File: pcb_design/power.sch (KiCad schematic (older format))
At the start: 0 parts

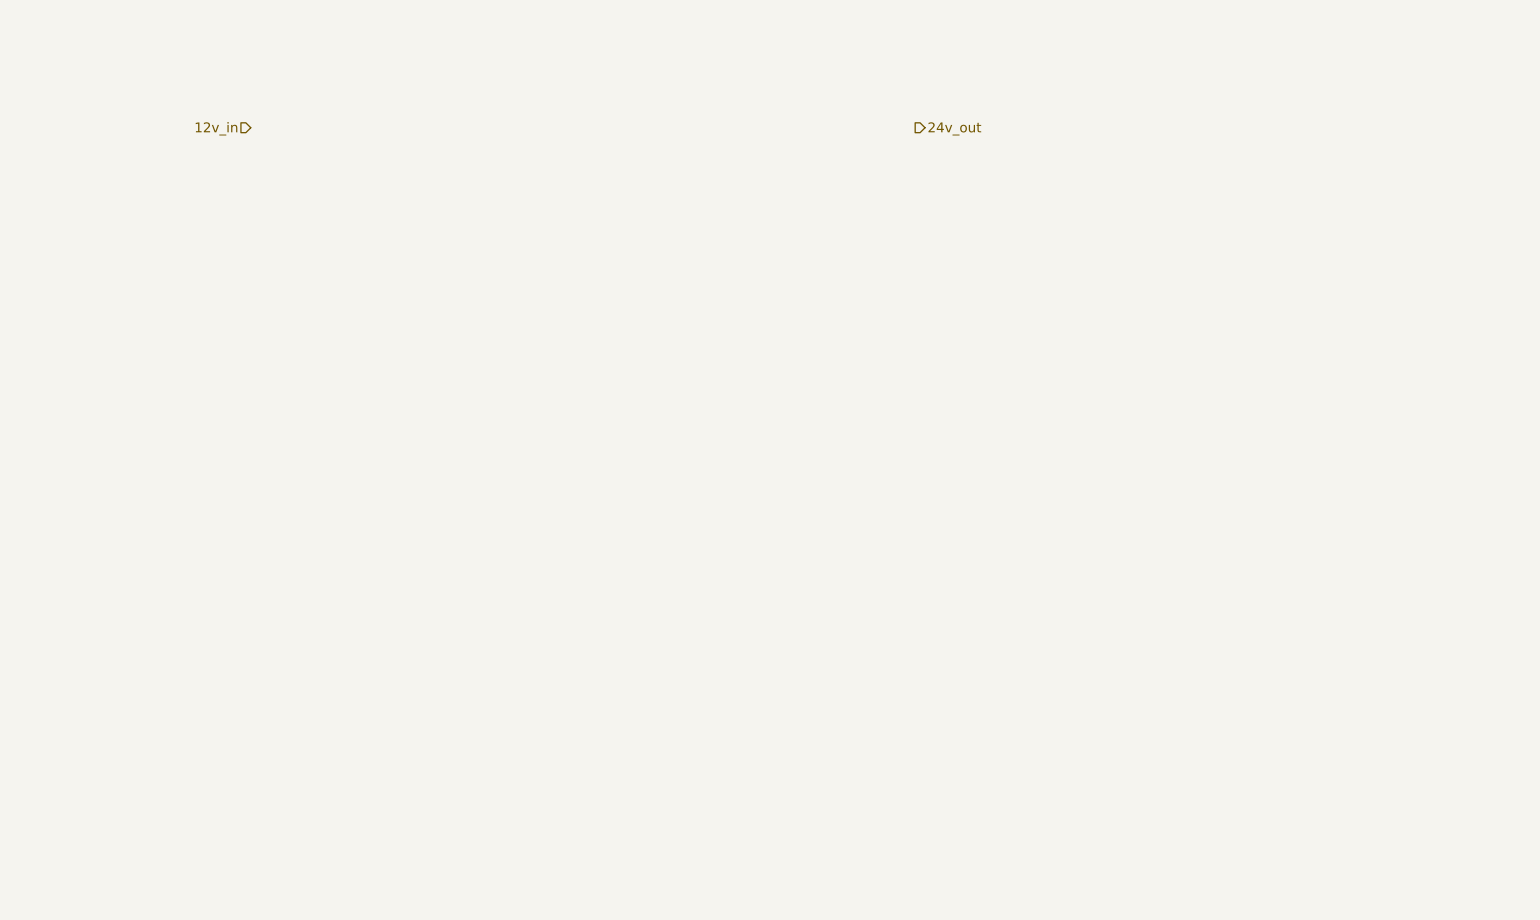
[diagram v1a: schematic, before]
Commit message: Added terminal blocks and power supplies
Signed-off-by: Marcos Chaparro <mchaparro@paltatech.com>
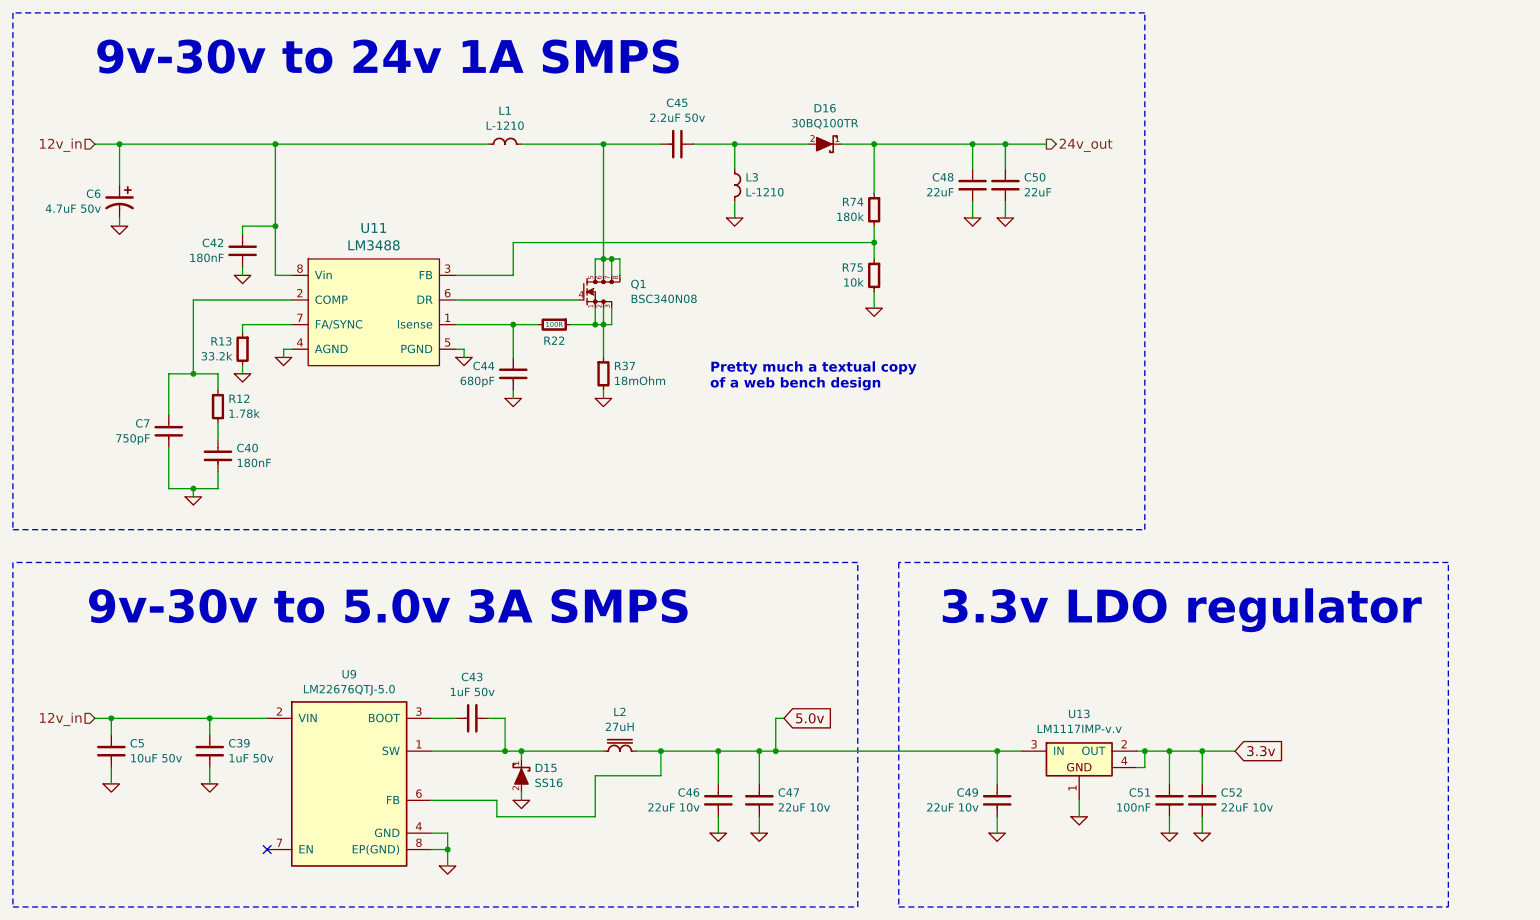
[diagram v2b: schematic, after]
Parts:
- added C39, C43: 1uF 50v, IPC7351-Nominal:CAPC2012X70, symbol C-0805
- added C40, C42: 180nF, IPC7351-Nominal:CAPC1608X55, symbol C-0603
- added C44: 680pF, IPC7351-Nominal:CAPC2012X70, symbol C-0805
- added C45: 2.2uF 50v, IPC7351-Nominal:CAPC3216X70, symbol C-1206
- added C46, C47, C49, C52: 22uF 10v, IPC7351-Nominal:CAPC3216X70, symbol C-1206
- added C48, C50: 22uF, IPC7351-Nominal:CAPC2012X70, symbol C-0805
- added C5: 10uF 50v, IPC7351-Nominal:CAPC3216X70, symbol C-1206
- added C51: 100nF, IPC7351-Nominal:CAPC1608X55, symbol C-0603
- added C6: 4.7uF 50v, IPC7351-Nominal:CAPMP7343X310, symbol C-TANT-7343-31
- added C7: 750pF, IPC7351-Nominal:CAPC2012X70, symbol C-0805
- added D15: SS16, IPC7351-Nominal:DIOM5326X292, symbol SS16
- added D16: 30BQ100TR, IPC7351-Nominal:DIOM7959X265, symbol MBRS360
- added L1, L3: L-1210, IPC7351-Nominal:INDC3225X135, symbol L-1210
- added L2: 27uH, manuf:BOURNS-SRP1238A, symbol L-BOURNS-SRN1060
- added Q1: BSC340N08, manuf:TEXAS-Q5A, symbol CSD18503Q5A
- added R12: 1.78k, IPC7351-Nominal:RESC1608X50, symbol R-0603
- added R13: 33.2k, IPC7351-Nominal:RESC1608X50, symbol R-0603
- added R22: 100R, IPC7351-Nominal:RESC1608X50, symbol R-0603
- added R37: 18mOhm, IPC7351-Nominal:CAPC1632X76, symbol R-0612
- added R74: 180k, IPC7351-Nominal:RESC1608X50, symbol R-0603
- added R75: 10k, IPC7351-Nominal:RESC1608X50, symbol R-0603
- added U11: LM3488, IPC7351-Nominal:SOP65P490X109-8, symbol LM3488
- added U13: LM1117IMP-v.v, smd-semi:SOT-223, symbol LM1117IMP-v.v
- added U9: LM22676QTJ-5.0, manuf:TO-263-7-TEXAS, symbol LM22676QTJ-5.0
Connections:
- net 12v_in: now also C39.1, C42.1, C5.1, C6.1, L1.2, U11.8 (Vin), U9.2 (VIN)
- net 24v_out: now also C48.1, C50.1, D16.1 (K), R74.1
- new net: C44.1, R22.2, U11.1 (Isense)
- new net: C7.1, R12.1, U11.2 (COMP)
- new net: R74.2, R75.1, U11.3 (FB)
- new net: Q1.4 (G), U11.6 (DR)
- new net: R13.1, U11.7 (FA/SYNC)
- new net: C40.1, R12.2
- new net: Q1.1 (S), Q1.2 (S), Q1.3 (S), R22.1, R37.1
- new net: C45.2, L1.1, Q1.5 (D), Q1.6 (D), Q1.7 (D), Q1.8 (D)
- new net: C45.1, D16.2 (A), L3.2
- new net: C43.1, D15.1 (K), L2.2, U9.1 (SW)
- new net: C43.2, U9.3 (BOOT)
- new net 3.3v: C51.1, C52.2, U13.2 (OUT), U13.4
- new net 5.0v: C46.1, C47.1, C49.1, L2.1, U13.3 (IN), U9.6 (FB)
- new net GND: C39.2, C40.2, C42.2, C44.2, C46.2, C47.2, C48.2, C49.2, C5.2, C50.2, C51.2, C52.1, C6.2, C7.2, D15.2 (A), L3.1, R13.2, R37.2, R75.2, U11.4 (AGND), U11.5 (PGND), U13.1, U9.4 (GND), U9.8 (EP(GND))
- no-connect marks 0 -> 1
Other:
- note added: "3.3v LDO regulator"
- note added: "9v-30v to 24v 1A SMPS"
- note added: "9v-30v to 5.0v 3A SMPS"
- note added: "Pretty much a textual copy\nof a web bench design"

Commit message: Added lp filters, fuses, tvs and power symbols
Signed-off-by: Marcos Chaparro <mchaparro@paltatech.com>
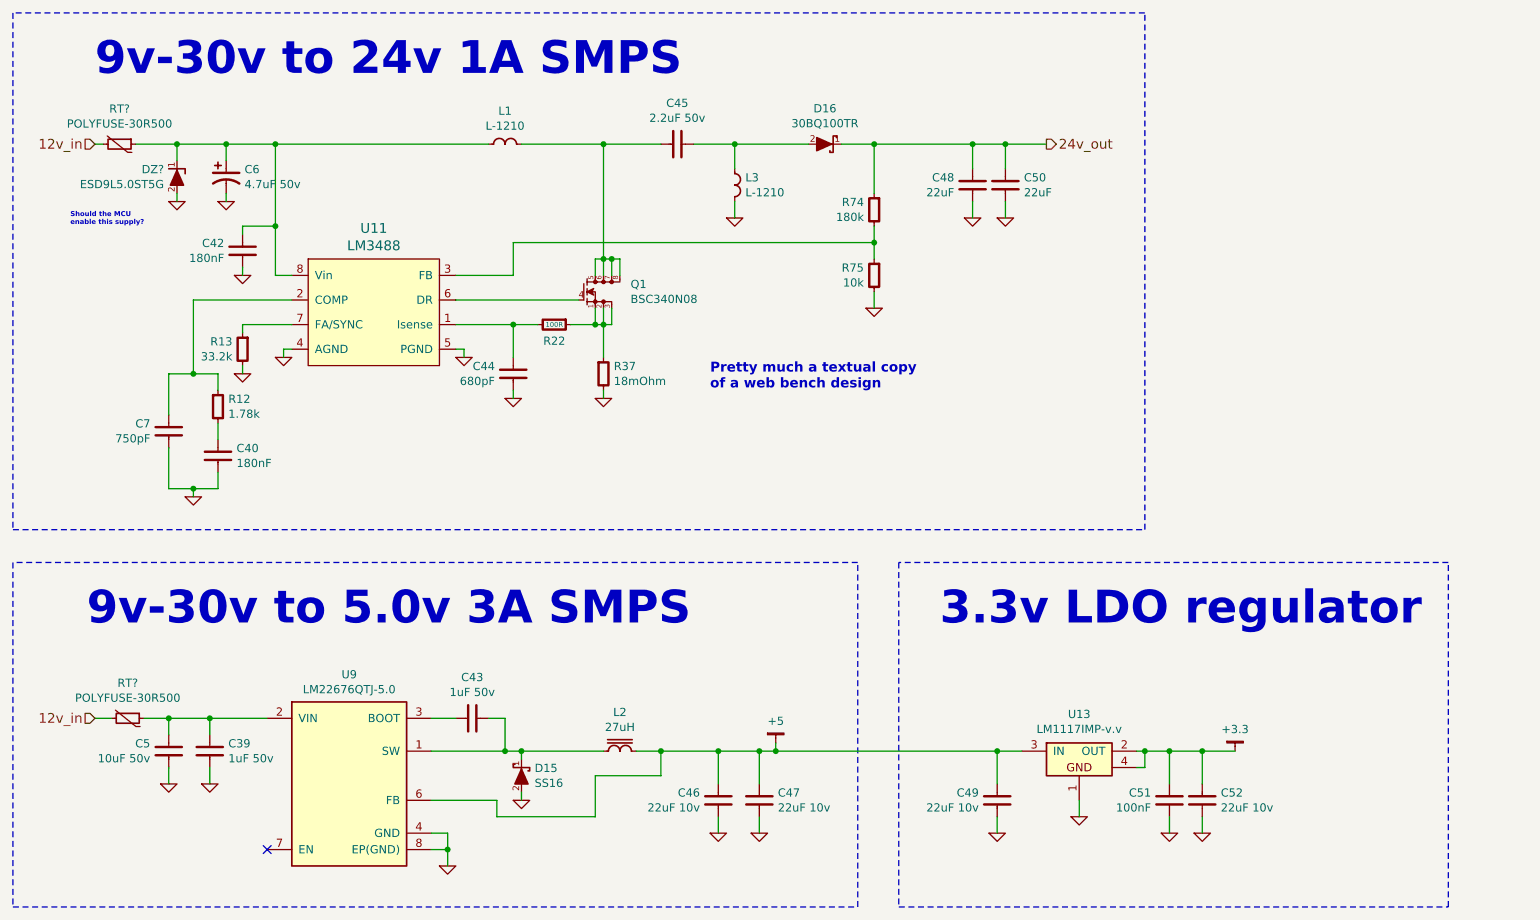
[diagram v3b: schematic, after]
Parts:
- added DZ?: ESD9L5.0ST5G, smd-semi:SOD-THAT, symbol ESD9L5.0ST5G
- added RT? (x2): POLYFUSE-30R500, manuf:LITTELFUSE-30R500, symbol POLYFUSE-30R500
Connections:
- net 12v_in: now also RT?.2, RT?.2; no longer C39.1, C42.1, C5.1, C6.1, L1.2, U11.8 (Vin), U9.2 (VIN)
- net GND: now also DZ?.2 (A)
- net 3.3v renamed +3.3
- net 5.0v renamed +5
- new net: C42.1, C6.1, DZ?.1 (K), L1.2, RT?.1, U11.8 (Vin)
- new net: C39.1, C5.1, RT?.1, U9.2 (VIN)
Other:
- note added: "Should the MCU\nenable this supply?"
- moved on the sheet: C5, C6

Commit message: Added bus voltage conditioning, %v to accel and regen inputs, regulator diode, annotated schematic
Signed-off-by: Marcos Chaparro <mchaparro@paltatech.com>
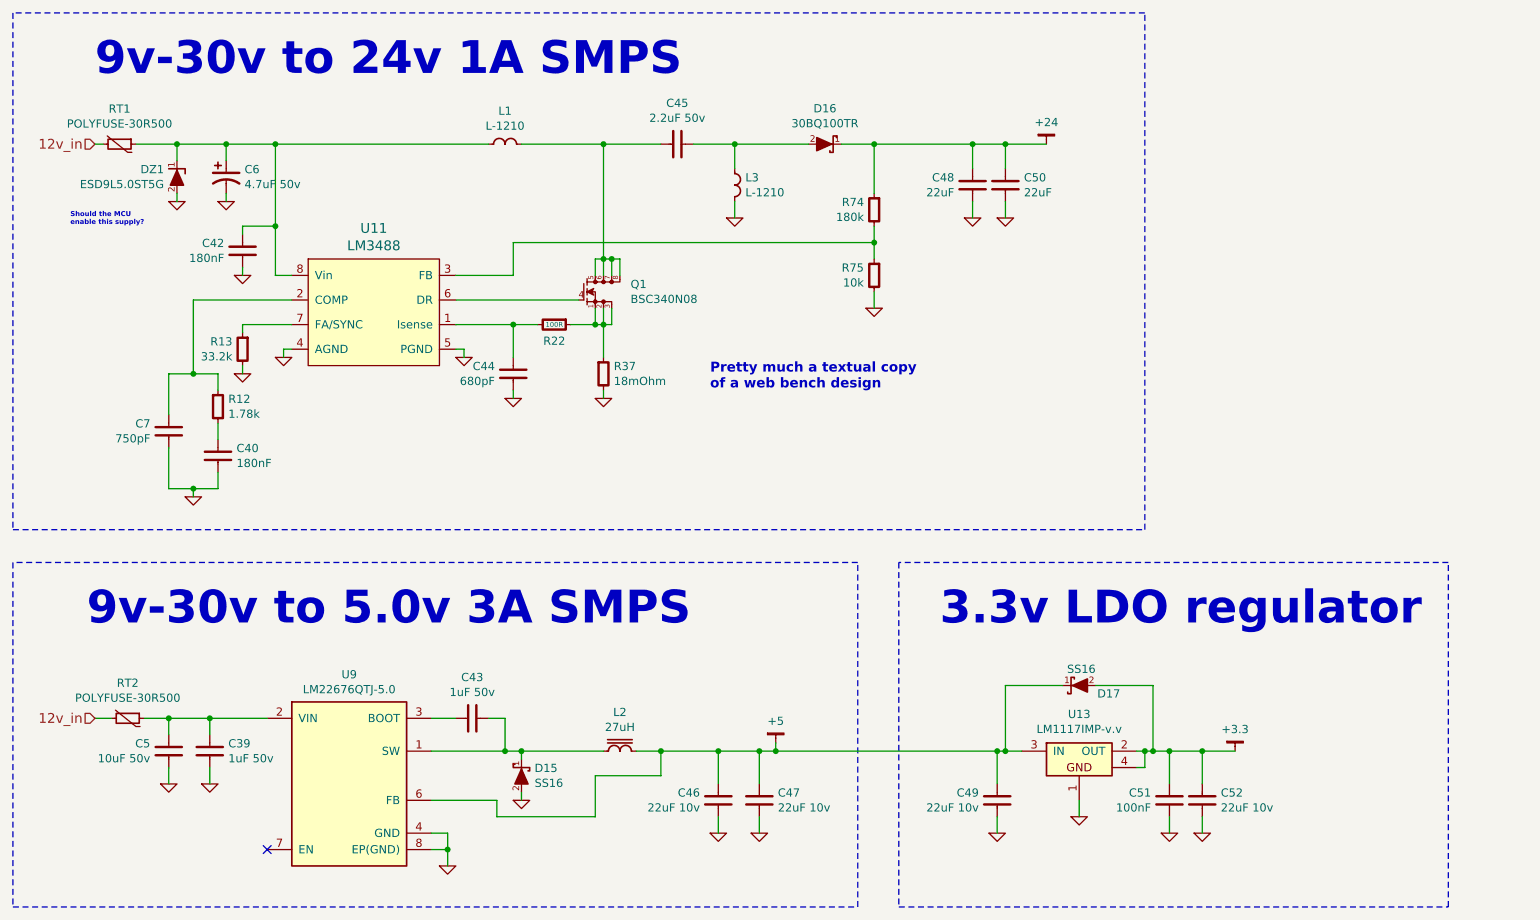
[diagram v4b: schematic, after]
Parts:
- added D17: SS16, IPC7351-Nominal:DIOM5326X292, symbol SS16
- gave numbers to parts that had none: 3
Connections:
- net +3.3: now also D17.2 (A)
- net +5: now also D17.1 (K)
- net 24v_out renamed +24

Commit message: Fixed issue with non-bidirectional phase current measurement. Started routing power supplies. Changed terminal blocks from 5.00mm to 3.81mm pitch
Signed-off-by: Marcos Chaparro <mchaparro@paltatech.com>
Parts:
- RT1, RT2: footprint manuf:LITTELFUSE-30R500 -> IPC7351-Most:RESC3216X60
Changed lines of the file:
@@
 Sheet 6 13
 Title "Power supplies"
-Date "2017-01-26"
-Rev "0"
-Comp ""
+Date "2017-01-24"
+Rev "0.1"
+Comp "vedder.se + PALTA TECH S.A. + PYMCO.fr"
 Comment1 ""
 Comment2 ""
@@
 Connection ~ 2100 4150
 $Comp
-L GND #PWR59
+L GND #PWR060
 U 1 1 588BC982
 P 2100 4200
-F 0 "#PWR59" H 2100 4200 30  0001 C CNN
+F 0 "#PWR060" H 2100 4200 30  0001 C CNN
 F 1 "GND" H 2100 4130 30  0001 C CNN
 F 2 "" H 2100 4200 60  0000 C CNN
@@
 	2400 3150 2400 3200
 $Comp
-L GND #PWR63
+L GND #PWR061
 U 1 1 588BD2D9
 P 2400 3450
-F 0 "#PWR63" H 2400 3450 30  0001 C CNN
+F 0 "#PWR061" H 2400 3450 30  0001 C CNN
 F 1 "GND" H 2400 3380 30  0001 C CNN
 F 2 "" H 2400 3450 60  0000 C CNN
@@
 	2400 3450 2400 3400
 $Comp
-L GND #PWR64
+L GND #PWR062
 U 1 1 588BD345
 P 2650 3350
-F 0 "#PWR64" H 2650 3350 30  0001 C CNN
+F 0 "#PWR062" H 2650 3350 30  0001 C CNN
 F 1 "GND" H 2650 3280 30  0001 C CNN
 F 2 "" H 2650 3350 60  0000 C CNN
@@
 	3750 3300 3750 3350
 $Comp
-L GND #PWR66
+L GND #PWR063
 U 1 1 588BD634
 P 3750 3350
-F 0 "#PWR66" H 3750 3350 30  0001 C CNN
+F 0 "#PWR063" H 3750 3350 30  0001 C CNN
 F 1 "GND" H 3750 3280 30  0001 C CNN
 F 2 "" H 3750 3350 60  0000 C CNN
@@
 	4050 3550 4050 3600
 $Comp
-L GND #PWR67
+L GND #PWR064
 U 1 1 588BDA1B
 P 4050 3600
-F 0 "#PWR67" H 4050 3600 30  0001 C CNN
+F 0 "#PWR064" H 4050 3600 30  0001 C CNN
 F 1 "GND" H 4050 3530 30  0001 C CNN
 F 2 "" H 4050 3600 60  0000 C CNN
@@
 	4600 3550 4600 3600
 $Comp
-L GND #PWR69
+L GND #PWR065
 U 1 1 588BDE06
 P 4600 3600
-F 0 "#PWR69" H 4600 3600 30  0001 C CNN
+F 0 "#PWR065" H 4600 3600 30  0001 C CNN
 F 1 "GND" H 4600 3530 30  0001 C CNN
 F 2 "" H 4600 3600 60  0000 C CNN
@@
 Connection ~ 2600 2550
 $Comp
-L GND #PWR62
+L GND #PWR066
 U 1 1 588BFA6D
 P 2400 2850
-F 0 "#PWR62" H 2400 2850 30  0001 C CNN
+F 0 "#PWR066" H 2400 2850 30  0001 C CNN
 F 1 "GND" H 2400 2780 30  0001 C CNN
 F 2 "" H 2400 2850 60  0000 C CNN
@@
 	2300 2150 2300 2050
 $Comp
-L GND #PWR61
+L GND #PWR067
 U 1 1 588C0261
 P 2300 2400
-F 0 "#PWR61" H 2300 2400 30  0001 C CNN
+F 0 "#PWR067" H 2300 2400 30  0001 C CNN
 F 1 "GND" H 2300 2330 30  0001 C CNN
 F 2 "" H 2300 2400 60  0000 C CNN
@@
 	5150 2050 5850 2050
 $Comp
-L GND #PWR71
+L GND #PWR068
 U 1 1 588C0D64
 P 5400 2500
-F 0 "#PWR71" H 5400 2500 30  0001 C CNN
+F 0 "#PWR068" H 5400 2500 30  0001 C CNN
 F 1 "GND" H 5400 2430 30  0001 C CNN
 F 2 "" H 5400 2500 60  0000 C CNN
@@
 	6050 2050 7300 2050
 $Comp
-L GND #PWR74
+L GND #PWR069
 U 1 1 588C18FD
 P 6250 3050
-F 0 "#PWR74" H 6250 3050 30  0001 C CNN
+F 0 "#PWR069" H 6250 3050 30  0001 C CNN
 F 1 "GND" H 6250 2980 30  0001 C CNN
 F 2 "" H 6250 3050 60  0000 C CNN
@@
 Connection ~ 6850 2050
 $Comp
-L GND #PWR75
+L GND #PWR070
 U 1 1 588C2312
 P 6850 2500
-F 0 "#PWR75" H 6850 2500 30  0001 C CNN
+F 0 "#PWR070" H 6850 2500 30  0001 C CNN
 F 1 "GND" H 6850 2430 30  0001 C CNN
 F 2 "" H 6850 2500 60  0000 C CNN
@@
 	6850 2500 6850 2400
 $Comp
-L GND #PWR77
+L GND #PWR071
 U 1 1 588C2433
 P 7050 2500
-F 0 "#PWR77" H 7050 2500 30  0001 C CNN
+F 0 "#PWR071" H 7050 2500 30  0001 C CNN
 F 1 "GND" H 7050 2430 30  0001 C CNN
 F 2 "" H 7050 2500 60  0000 C CNN
@@
 Connection ~ 2200 5550
 $Comp
-L GND #PWR57
+L GND #PWR072
 U 1 1 588C4382
 P 1950 5950
-F 0 "#PWR57" H 1950 5950 30  0001 C CNN
+F 0 "#PWR072" H 1950 5950 30  0001 C CNN
 F 1 "GND" H 1950 5880 30  0001 C CNN
 F 2 "" H 1950 5950 60  0000 C CNN
@@
 	1950 5950 1950 5850
 $Comp
-L GND #PWR60
+L GND #PWR073
 U 1 1 588C4468
 P 2200 5950
-F 0 "#PWR60" H 2200 5950 30  0001 C CNN
+F 0 "#PWR073" H 2200 5950 30  0001 C CNN
 F 1 "GND" H 2200 5880 30  0001 C CNN
 F 2 "" H 2200 5950 60  0000 C CNN
@@
 Connection ~ 4000 5750
 $Comp
-L GND #PWR68
+L GND #PWR074
 U 1 1 588C56F7
 P 4100 6050
-F 0 "#PWR68" H 4100 6050 30  0001 C CNN
+F 0 "#PWR074" H 4100 6050 30  0001 C CNN
 F 1 "GND" H 4100 5980 30  0001 C CNN
 F 2 "" H 4100 6050 60  0000 C CNN
@@
 Connection ~ 5300 5750
 $Comp
-L GND #PWR70
+L GND #PWR075
 U 1 1 588C63EB
 P 5300 6250
-F 0 "#PWR70" H 5300 6250 30  0001 C CNN
+F 0 "#PWR075" H 5300 6250 30  0001 C CNN
 F 1 "GND" H 5300 6180 30  0001 C CNN
 F 2 "" H 5300 6250 60  0000 C CNN
@@
 $EndComp
 $Comp
-L GND #PWR72
+L GND #PWR076
 U 1 1 588C6447
 P 5550 6250
-F 0 "#PWR72" H 5550 6250 30  0001 C CNN
+F 0 "#PWR076" H 5550 6250 30  0001 C CNN
 F 1 "GND" H 5550 6180 30  0001 C CNN
 F 2 "" H 5550 6250 60  0000 C CNN
@@
 NoConn ~ 2550 6350
 $Comp
-L GND #PWR65
+L GND #PWR077
 U 1 1 588C6DC2
 P 3650 6450
-F 0 "#PWR65" H 3650 6450 30  0001 C CNN
+F 0 "#PWR077" H 3650 6450 30  0001 C CNN
 F 1 "GND" H 3650 6380 30  0001 C CNN
 F 2 "" H 3650 6450 60  0000 C CNN
@@
 Connection ~ 7000 5750
 $Comp
-L GND #PWR76
+L GND #PWR078
 U 1 1 588C792B
 P 7000 6250
-F 0 "#PWR76" H 7000 6250 30  0001 C CNN
+F 0 "#PWR078" H 7000 6250 30  0001 C CNN
 F 1 "GND" H 7000 6180 30  0001 C CNN
 F 2 "" H 7000 6250 60  0000 C CNN
@@
 	7000 6250 7000 6150
 $Comp
-L GND #PWR79
+L GND #PWR079
 U 1 1 588C79EC
 P 7500 6150
-F 0 "#PWR79" H 7500 6150 30  0001 C CNN
+F 0 "#PWR079" H 7500 6150 30  0001 C CNN
 F 1 "GND" H 7500 6080 30  0001 C CNN
 F 2 "" H 7500 6150 60  0000 C CNN
@@
 Connection ~ 8050 5750
 $Comp
-L GND #PWR80
+L GND #PWR080
 U 1 1 588C813C
 P 8050 6250
-F 0 "#PWR80" H 8050 6250 30  0001 C CNN
+F 0 "#PWR080" H 8050 6250 30  0001 C CNN
 F 1 "GND" H 8050 6180 30  0001 C CNN
 F 2 "" H 8050 6250 60  0000 C CNN
@@
 	8050 6250 8050 6150
 $Comp
-L GND #PWR81
+L GND #PWR081
 U 1 1 588C81BF
 P 8250 6250
-F 0 "#PWR81" H 8250 6250 30  0001 C CNN
+F 0 "#PWR081" H 8250 6250 30  0001 C CNN
 F 1 "GND" H 8250 6180 30  0001 C CNN
 F 2 "" H 8250 6250 60  0000 C CNN
@@
 	9750 4600 6400 4600
 $Comp
-L +3.3 #PWR82
+L +3.3 #PWR082
 U 1 1 588BD2B2
 P 8450 5750
-F 0 "#PWR82" H 8500 5800 30  0001 C CNN
+F 0 "#PWR082" H 8500 5800 30  0001 C CNN
 F 1 "+3.3" H 8450 5883 50  0000 C CNN
 F 2 "" H -100 0   60  0000 C CNN
@@
 $EndComp
 $Comp
-L +5 #PWR73
+L +5 #PWR083
 U 1 1 588BD705
 P 5650 5700
-F 0 "#PWR73" H 5700 5750 30  0001 C CNN
+F 0 "#PWR083" H 5700 5750 30  0001 C CNN
 F 1 "+5" H 5650 5833 50  0000 C CNN
 F 2 "" H -400 50  60  0000 C CNN
@@
 F 0 "RT1" V 1435 2050 50  0000 C CNN
 F 1 "POLYFUSE-30R500" V 1526 2050 50  0000 C CNN
-F 2 "manuf:LITTELFUSE-30R500" H 150 -1000 60  0001 C CNN
+F 2 "IPC7351-Most:RESC3216X60" H 150 -1000 60  0001 C CNN
 F 3 "" H 150 -1100 60  0000 C CNN
 F 4 "PTC LITTELFUSE 30R500" H 800 -600 60  0001 C CNN "BOM"
@@
 Connection ~ 2000 2050
 $Comp
-L GND #PWR58
+L GND #PWR084
 U 1 1 588CB9A0
 P 2000 2400
-F 0 "#PWR58" H 2000 2400 30  0001 C CNN
+F 0 "#PWR084" H 2000 2400 30  0001 C CNN
 F 1 "GND" H 2000 2330 30  0001 C CNN
 F 2 "" H 2000 2400 60  0000 C CNN
@@
 F 0 "RT2" V 1485 5550 50  0000 C CNN
 F 1 "POLYFUSE-30R500" V 1576 5550 50  0000 C CNN
-F 2 "manuf:LITTELFUSE-30R500" H 200 2500 60  0001 C CNN
+F 2 "IPC7351-Most:RESC3216X60" H 200 2500 60  0001 C CNN
 F 3 "" H 200 2400 60  0000 C CNN
 F 4 "PTC LITTELFUSE 30R500" H 850 2900 60  0001 C CNN "BOM"
@@
 Connection ~ 7050 5750
 $Comp
-L +24 #PWR78
+L +24 #PWR085
 U 1 1 588CFB19
 P 7300 2050
-F 0 "#PWR78" H -100 50  30  0001 C CNN
+F 0 "#PWR085" H -100 50  30  0001 C CNN
 F 1 "+24" H 7300 2183 50  0000 C CNN
 F 2 "" H -100 0   60  0000 C CNN
